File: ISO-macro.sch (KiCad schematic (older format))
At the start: 26 parts, among them J1 USB_C_Receptacle_USB2.0, SW1 SW_SPST, SW2 SW_SPST, SW3 SW_SPST, SW4 SW_SPST, SW5 SW_SPST, SW6 SW_SPST, SW7 SW_SPST, SW8 EC11, SW9 SW_SPST, U1 ATmega16U2-MU, Y1 Resonator

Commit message: wip
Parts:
- J1: symbol Connector:USB_C_Receptacle_USB2.0 -> ISO-macro-rescue:USB_C_Receptacle_USB2.0-Connector
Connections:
- wire segments 85 -> 73
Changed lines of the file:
@@
 $EndComp
 $Comp
-L Connector:USB_C_Receptacle_USB2.0 J1
+L ISO-macro-rescue:USB_C_Receptacle_USB2.0-Connector J1
 U 1 1 60B90A6D
 P 1250 1750
@@
 Wire Wire Line
 	1850 1150 2000 1150
-Wire Wire Line
-	4450 4350 4800 4350
-Wire Wire Line
-	4450 4650 4800 4650
-Wire Wire Line
-	4450 4750 5000 4750
-Wire Wire Line
-	4450 3150 4850 3150
-Wire Wire Line
-	4450 3250 5000 3250
-Wire Wire Line
-	4450 3650 4850 3650
-$Comp
-L power:GND #PWR0112
-U 1 1 60C6780B
-P 5650 3150
-F 0 "#PWR0112" H 5650 2900 50  0001 C CNN
-F 1 "GND" V 5655 3022 50  0000 R CNN
-F 2 "" H 5650 3150 50  0001 C CNN
-F 3 "" H 5650 3150 50  0001 C CNN
-	1    5650 3150
-	1    0    0    -1
-$EndComp
-$Comp
-L power:GND #PWR0114
-U 1 1 60C688DF
-P 4850 3350
-F 0 "#PWR0114" H 4850 3100 50  0001 C CNN
-F 1 "GND" V 4855 3222 50  0000 R CNN
-F 2 "" H 4850 3350 50  0001 C CNN
-F 3 "" H 4850 3350 50  0001 C CNN
-	1    4850 3350
-	0    -1   -1   0
-$EndComp
-$Comp
-L power:GND #PWR0115
-U 1 1 60C690EB
-P 5550 3650
-F 0 "#PWR0115" H 5550 3400 50  0001 C CNN
-F 1 "GND" V 5555 3522 50  0000 R CNN
-F 2 "" H 5550 3650 50  0001 C CNN
-F 3 "" H 5550 3650 50  0001 C CNN
-	1    5550 3650
-	1    0    0    -1
-$EndComp
-$Comp
-L power:GND #PWR0117
-U 1 1 60C6A4A2
-P 5550 4350
-F 0 "#PWR0117" H 5550 4100 50  0001 C CNN
-F 1 "GND" V 5555 4222 50  0000 R CNN
-F 2 "" H 5550 4350 50  0001 C CNN
-F 3 "" H 5550 4350 50  0001 C CNN
-	1    5550 4350
-	1    0    0    -1
-$EndComp
-$Comp
-L power:GND #PWR0118
-U 1 1 60C6A762
-P 5650 4650
-F 0 "#PWR0118" H 5650 4400 50  0001 C CNN
-F 1 "GND" V 5655 4522 50  0000 R CNN
-F 2 "" H 5650 4650 50  0001 C CNN
-F 3 "" H 5650 4650 50  0001 C CNN
-	1    5650 4650
-	1    0    0    -1
-$EndComp
-$Comp
-L power:GND #PWR0119
-U 1 1 60C6AA14
-P 5750 4750
-F 0 "#PWR0119" H 5750 4500 50  0001 C CNN
-F 1 "GND" V 5755 4622 50  0000 R CNN
-F 2 "" H 5750 4750 50  0001 C CNN
-F 3 "" H 5750 4750 50  0001 C CNN
-	1    5750 4750
-	1    0    0    -1
-$EndComp
 $Comp
 L LED:WS2812B D1
@@
 NoConn ~ 1850 2250
 NoConn ~ 1850 2350
-Text Label 4450 3750 0    50   ~ 0
+Text Label 4450 4750 0    50   ~ 0
 encsw
 Text Label 6750 1950 2    50   ~ 0
@@
 	1    0    0    -1
 $EndComp
-Text Label 4450 4150 0    50   ~ 0
+Text Label 4450 4650 0    50   ~ 0
 EncB
 Text Label 4450 4050 0    50   ~ 0
 EncA
-$Comp
-L power:GND #PWR0113
-U 1 1 60C6836C
-P 5550 3250
-F 0 "#PWR0113" H 5550 3000 50  0001 C CNN
-F 1 "GND" V 5555 3122 50  0000 R CNN
-F 2 "" H 5550 3250 50  0001 C CNN
-F 3 "" H 5550 3250 50  0001 C CNN
-	1    5550 3250
-	1    0    0    -1
-$EndComp
-Wire Wire Line
-	5400 3250 5550 3250
-Wire Wire Line
-	5250 3150 5650 3150
-Wire Wire Line
-	5250 3650 5550 3650
-Wire Wire Line
-	5200 4350 5550 4350
-Wire Wire Line
-	5200 4650 5650 4650
-Wire Wire Line
-	5400 4750 5750 4750
 Text Label 4850 5350 3    50   ~ 0
 LED

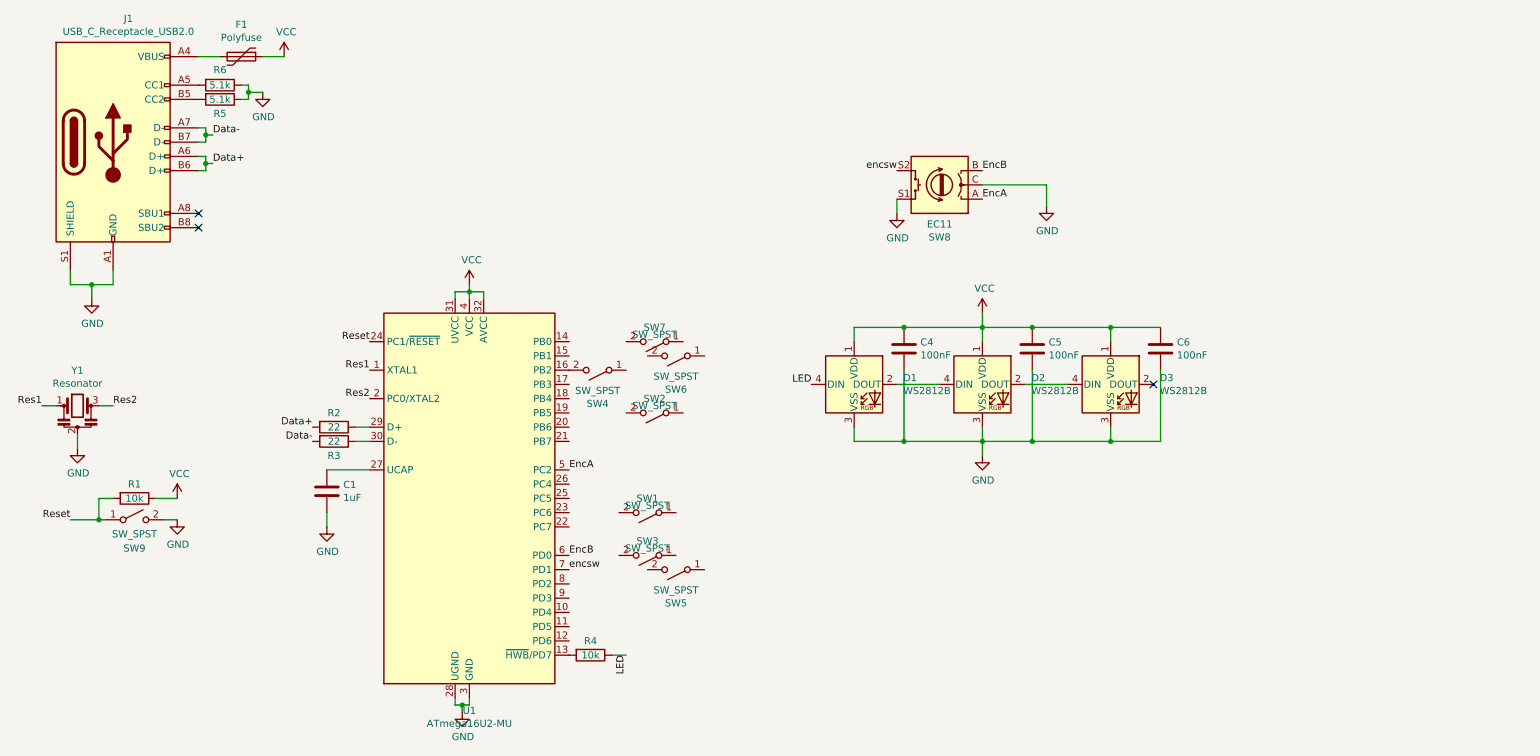
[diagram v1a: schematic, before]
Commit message: Add LEDs and power caps, routing
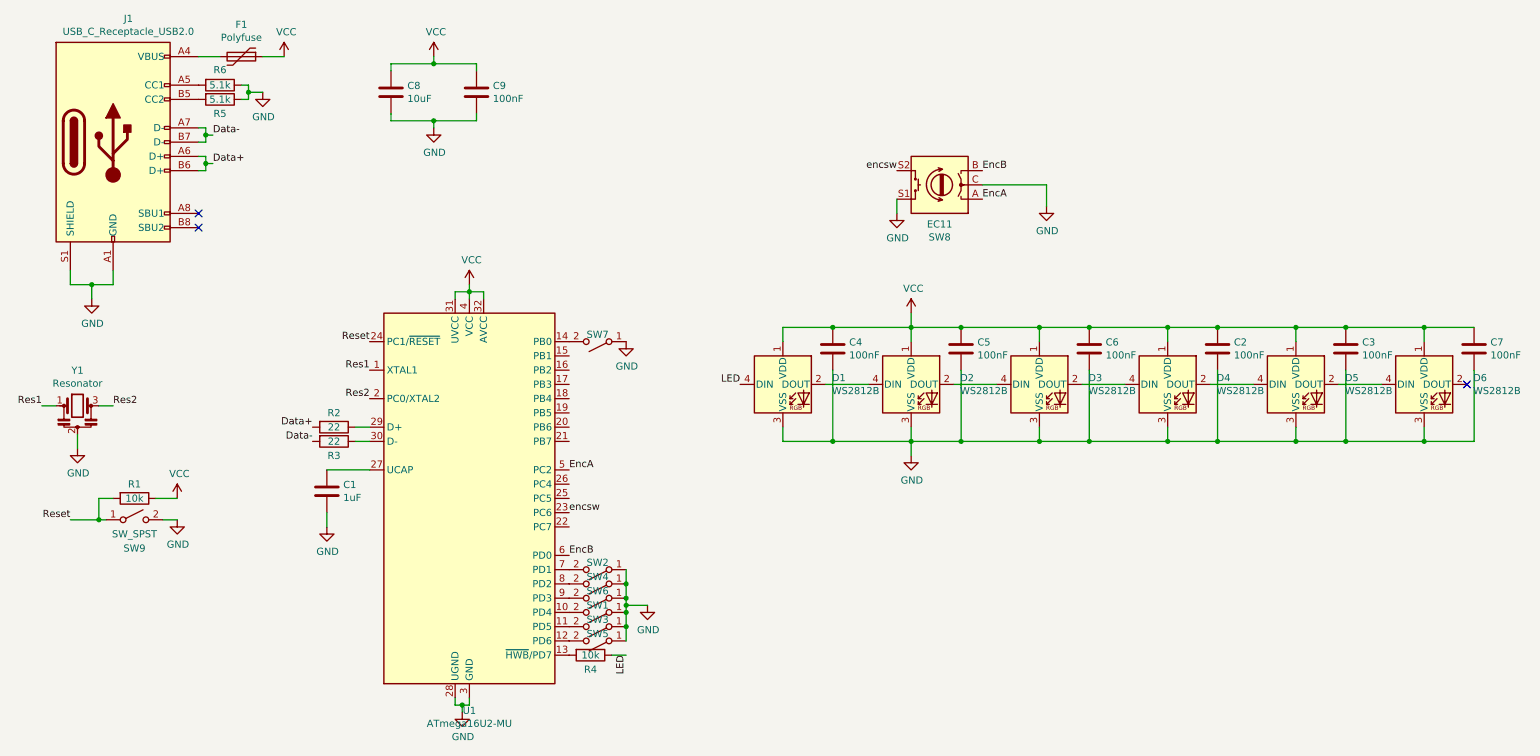
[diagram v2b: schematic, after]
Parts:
- added C2, C3, C7, C9: 100nF, Capacitor_SMD:C_0402_1005Metric, symbol Device:C
- added C8: 10uF, Capacitor_SMD:C_0402_1005Metric, symbol Device:C
- added D4, D5, D6: WS2812B, LED_SMD:LED_SK6812MINI_PLCC4_3.5x3.5mm_P1.75mm, symbol LED:WS2812B
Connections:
- net GND: now also SW1.1 (A), SW2.1 (A), SW3.1 (A), SW4.1 (A), SW5.1 (A), SW6.1 (A), SW7.1 (A), C2.2, C3.2, C7.2, C8.2, C9.2, D4.3 (VSS), D5.3 (VSS), D6.3 (VSS)
- net VCC: now also C2.1, C3.1, C7.1, C8.1, C9.1, D4.1 (VDD), D5.1 (VDD), D6.1 (VDD)
- net encsw: now also U1.23 (PC6); no longer U1.7 (PD1)
- net at SW3.2 (B): now also U1.11 (PD5)
- net at SW5.2 (B): now also U1.12 (PD6)
- net at SW7.2 (B): now also U1.14 (PB0)
- net at SW6.2 (B): now also U1.9 (PD3)
- net at SW4.2 (B): now also U1.8 (PD2); no longer U1.16 (PB2)
- net at SW2.2 (B): now also U1.7 (PD1)
- net at SW1.2 (B): now also U1.10 (PD4)
- net at D3.2 (DOUT): now also D4.4 (DIN)
- new net: D4.2 (DOUT), D5.4 (DIN)
- new net: D5.2 (DOUT), D6.4 (DIN)
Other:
- moved on the sheet: C4, C5, C6, D1, D2, D3, SW1, SW2, SW3, SW4, SW5, SW6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

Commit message: Add NCs where appropriate
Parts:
- J1: symbol ISO-macro-rescue:USB_C_Receptacle_USB2.0-Connector -> ISO-macro-rescue:USB_C_Receptacle_USB2.0-Connector-ISO-macro-rescue
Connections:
- no-connect marks 3 -> 13
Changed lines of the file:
@@
 $EndComp
 $Comp
-L ISO-macro-rescue:USB_C_Receptacle_USB2.0-Connector J1
+L ISO-macro-rescue:USB_C_Receptacle_USB2.0-Connector-ISO-macro-rescue J1
 U 1 1 60B90A6D
 P 1250 1750
@@
 Wire Wire Line
 	3800 1600 3800 1550
+NoConn ~ 4450 3250
+NoConn ~ 4450 3350
+NoConn ~ 4450 3450
+NoConn ~ 4450 3550
+NoConn ~ 4450 3650
+NoConn ~ 4450 3750
+NoConn ~ 4450 3850
+NoConn ~ 4450 4150
+NoConn ~ 4450 4250
+NoConn ~ 4450 4450
 $EndSCHEMATC
